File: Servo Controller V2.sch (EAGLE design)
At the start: 36 parts, among them P1 Power, IO, P2 Servo, P3 Program, Q1 BSS138, Q2 IRLML9301TRPBF, U1 ATTINY402-SSNR, U2 TPS82140SILR, U3 MCP1754ST-3302E_CB, U4 MCP1754ST-3302E_CB

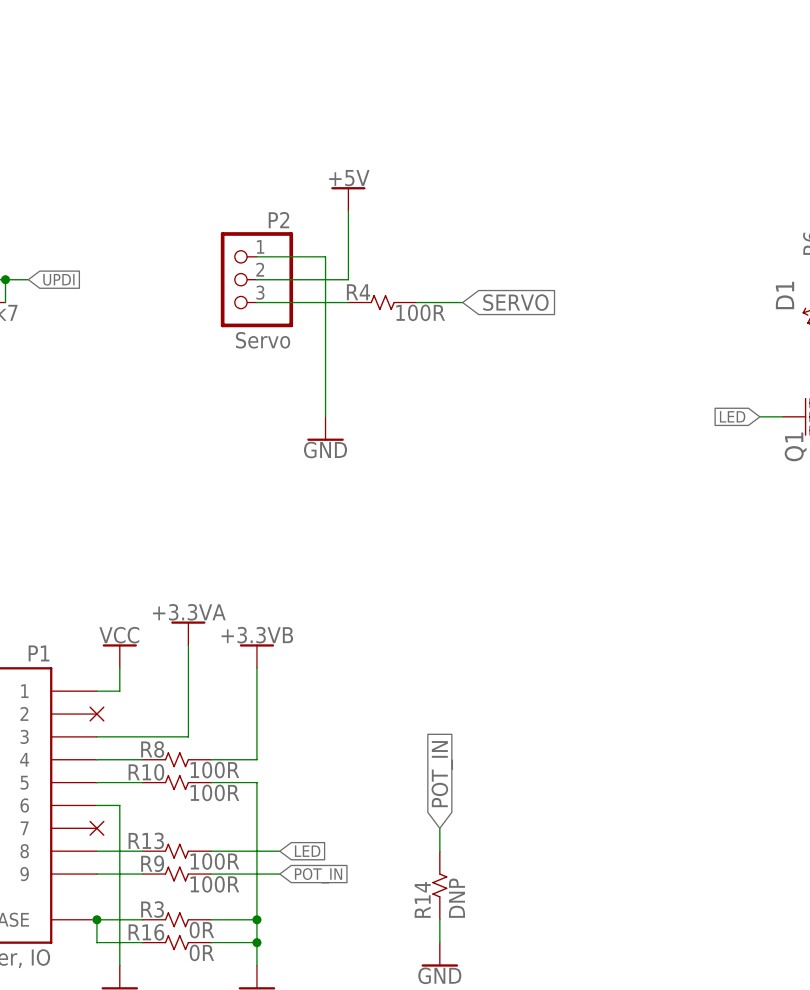
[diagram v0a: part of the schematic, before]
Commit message: Eliminated back EMI on the 5V rail from a large motor braking.
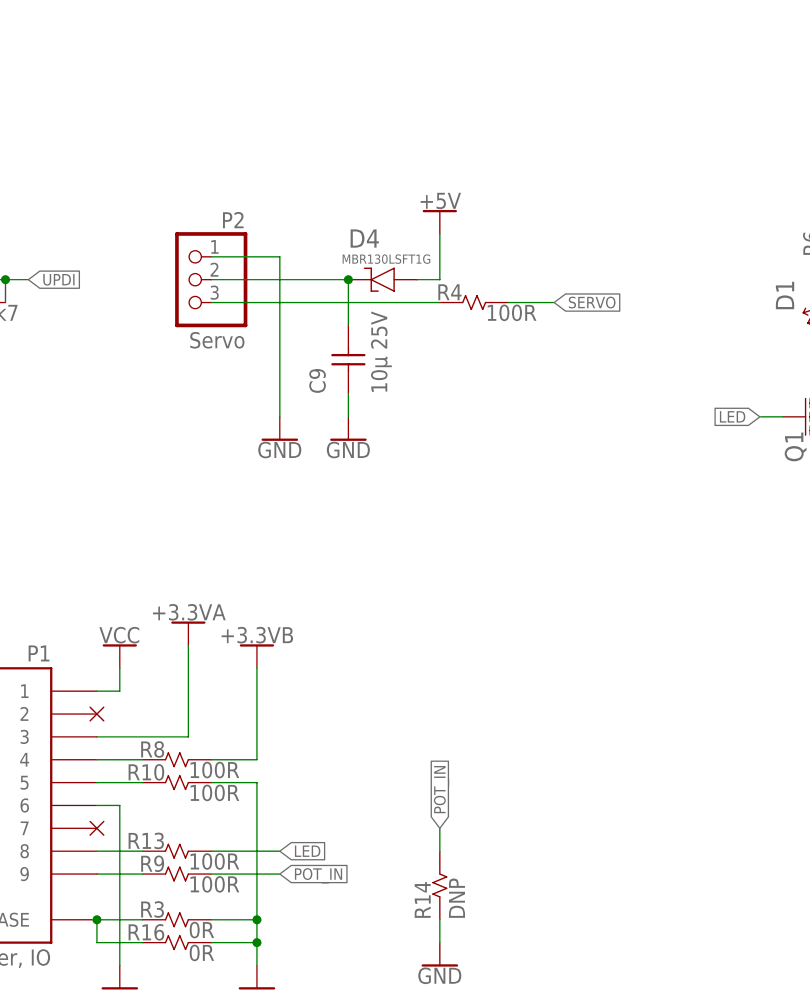
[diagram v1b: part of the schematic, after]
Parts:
- added C9: 10µ 25V, lcr:CAPACITOR-1206
- added D4: MBR130LSFT1G, lcr:DIODE-SCHOTTKY-ON-MBR130LSFT1G
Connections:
- new net N$19: C9.P$2, D4.C, P2.2
- net +5V: now also D4.A; no longer P2.2
- net GND: now also C9.P$1
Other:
- moved on the sheet: P2, R4
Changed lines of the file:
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@@
 <drawing>
 <settings>
-<setting alwaysvectorfont="no"/>
+<setting alwaysvectorfont="yes"/>
 <setting verticaltext="up"/>
 </settings>
@@
 <part name="P19" library="supply" library_urn="urn:adsk.eagle:library:8729613" deviceset="+5V" device=""/>
 <part name="P20" library="supply" library_urn="urn:adsk.eagle:library:8729613" deviceset="+5V" device=""/>
+<part name="C9" library="lcr" library_urn="urn:adsk.eagle:library:3920968" deviceset="CAPACITOR" device="-1206" package3d_urn="urn:adsk.eagle:package:4274891/1" value="10µ 25V"/>
+<part name="D4" library="lcr" library_urn="urn:adsk.eagle:library:3920968" deviceset="DIODE-SCHOTTKY" device="-ON-MBR130LSFT1G" package3d_urn="urn:adsk.eagle:package:4270842/1" value="MBR130LSFT1G"/>
+<part name="GND20" library="supply1" library_urn="urn:adsk.eagle:library:371" deviceset="GND" device=""/>
 </parts>
 <sheets>
@@
 <attribute name="VALUE" x="68.58" y="168.402" size="1.778" layer="96"/>
 </instance>
-<instance part="P2" gate="A" x="63.5" y="93.98" smashed="yes" rot="MR0">
-<attribute name="NAME" x="69.85" y="99.695" size="1.778" layer="95" rot="MR0"/>
-<attribute name="VALUE" x="69.85" y="86.36" size="1.778" layer="96" rot="MR0"/>
+<instance part="P2" gate="A" x="58.42" y="93.98" smashed="yes" rot="MR0">
+<attribute name="NAME" x="64.77" y="99.695" size="1.778" layer="95" rot="MR0"/>
+<attribute name="VALUE" x="64.77" y="86.36" size="1.778" layer="96" rot="MR0"/>
 </instance>
 <instance part="R1" gate="G$1" x="190.5" y="60.96" smashed="yes">
@@
 <attribute name="VALUE" x="248.92" y="55.626" size="1.778" layer="96" align="top-center"/>
 </instance>
-<instance part="GND12" gate="1" x="73.66" y="76.2" smashed="yes">
-<attribute name="VALUE" x="73.66" y="75.946" size="1.778" layer="96" align="top-center"/>
+<instance part="GND12" gate="1" x="68.58" y="76.2" smashed="yes">
+<attribute name="VALUE" x="68.58" y="75.946" size="1.778" layer="96" align="top-center"/>
 </instance>
 <instance part="GND13" gate="1" x="27.94" y="76.2" smashed="yes">
@@
 <attribute name="VALUE" x="58.42" y="36.068" size="1.778" layer="96"/>
 </instance>
-<instance part="R4" gate="G$1" x="81.28" y="91.44" smashed="yes">
-<attribute name="NAME" x="78.74" y="91.694" size="1.778" layer="95" rot="MR0"/>
-<attribute name="VALUE" x="81.28" y="89.408" size="1.778" layer="96"/>
+<instance part="R4" gate="G$1" x="91.44" y="91.44" smashed="yes">
+<attribute name="NAME" x="88.9" y="91.694" size="1.778" layer="95" rot="MR0"/>
+<attribute name="VALUE" x="91.44" y="89.408" size="1.778" layer="96"/>
 </instance>
 <instance part="R3" gate="G$1" x="58.42" y="22.86" smashed="yes">
@@
 <instance part="P17" gate="G$1" x="157.48" y="170.18" smashed="yes"/>
 <instance part="P18" gate="G$1" x="58.42" y="170.18" smashed="yes"/>
-<instance part="P19" gate="G$1" x="76.2" y="104.14" smashed="yes"/>
+<instance part="P19" gate="G$1" x="86.36" y="101.6" smashed="yes"/>
 <instance part="P20" gate="G$1" x="137.16" y="111.76" smashed="yes"/>
+<instance part="C9" gate="G$1" x="76.2" y="83.82" smashed="yes" rot="R90">
+<attribute name="NAME" x="73.66" y="81.28" size="1.778" layer="95" rot="R90"/>
+<attribute name="VALUE" x="80.518" y="81.28" size="1.778" layer="96" rot="R90"/>
+</instance>
+<instance part="D4" gate="G$1" x="81.28" y="93.98" smashed="yes" rot="MR0">
+<attribute name="NAME" x="76.2" y="97.536" size="2.032" layer="95"/>
+<attribute name="VALUE" x="75.438" y="95.758" size="1.016" layer="96"/>
+</instance>
+<instance part="GND20" gate="1" x="76.2" y="76.2" smashed="yes">
+<attribute name="VALUE" x="76.2" y="75.946" size="1.778" layer="96" align="top-center"/>
+</instance>
 </instances>
 <busses>
@@
 <pinref part="P2" gate="A" pin="1"/>
 <pinref part="GND12" gate="1" pin="GND"/>
-<wire x1="66.04" y1="96.52" x2="73.66" y2="96.52" width="0.1524" layer="91"/>
-<wire x1="73.66" y1="96.52" x2="73.66" y2="78.74" width="0.1524" layer="91"/>
+<wire x1="60.96" y1="96.52" x2="68.58" y2="96.52" width="0.1524" layer="91"/>
+<wire x1="68.58" y1="96.52" x2="68.58" y2="78.74" width="0.1524" layer="91"/>
 </segment>
 <segment>
@@
 <wire x1="22.86" y1="144.78" x2="22.86" y2="147.32" width="0.1524" layer="91"/>
 </segment>
+<segment>
+<pinref part="C9" gate="G$1" pin="P$1"/>
+<wire x1="76.2" y1="81.28" x2="76.2" y2="78.74" width="0.1524" layer="91"/>
+<pinref part="GND20" gate="1" pin="GND"/>
+</segment>
 </net>
 <net name="UPDI" class="0">
@@
 <wire x1="38.1" y1="93.98" x2="40.64" y2="93.98" width="0.1524" layer="91"/>
 <junction x="38.1" y="93.98"/>
-<label x="40.64" y="93.98" size="1.27" layer="255" xref="yes"/>
+<label x="40.64" y="93.98" size="1.27" layer="95" xref="yes"/>
 </segment>
 </net>
@@
 <pinref part="U1" gate="G$1" pin="PA7"/>
 <wire x1="193.04" y1="88.9" x2="187.96" y2="88.9" width="0.1524" layer="91"/>
-<label x="187.96" y="88.9" size="1.27" layer="255" rot="R180" xref="yes"/>
+<label x="187.96" y="88.9" size="1.27" layer="95" rot="R180" xref="yes"/>
 </segment>
 <segment>
@@
 <wire x1="218.44" y1="63.5" x2="218.44" y2="66.04" width="0.1524" layer="91"/>
 <wire x1="218.44" y1="66.04" x2="226.06" y2="66.04" width="0.1524" layer="91"/>
-<label x="226.06" y="66.04" size="1.27" layer="255" xref="yes"/>
+<label x="226.06" y="66.04" size="1.27" layer="95" xref="yes"/>
 </segment>
 </net>
@@
 <pinref part="U1" gate="G$1" pin="PA6"/>
 <wire x1="193.04" y1="91.44" x2="187.96" y2="91.44" width="0.1524" layer="91"/>
-<label x="187.96" y="91.44" size="1.27" layer="255" rot="R180" xref="yes"/>
+<label x="187.96" y="91.44" size="1.27" layer="95" rot="R180" xref="yes"/>
 </segment>
 <segment>
@@
 <wire x1="190.5" y1="63.5" x2="190.5" y2="66.04" width="0.1524" layer="91"/>
 <wire x1="190.5" y1="66.04" x2="198.12" y2="66.04" width="0.1524" layer="91"/>
-<label x="198.12" y="66.04" size="1.27" layer="255" xref="yes"/>
+<label x="198.12" y="66.04" size="1.27" layer="95" xref="yes"/>
 </segment>
 </net>
 <net name="POT_IN" class="0">
 <segment>
-<label x="187.96" y="86.36" size="1.27" layer="255" rot="R180" xref="yes"/>
+<label x="187.96" y="86.36" size="1.27" layer="95" rot="R180" xref="yes"/>
 <pinref part="U1" gate="G$1" pin="PA1"/>
 <wire x1="187.96" y1="86.36" x2="193.04" y2="86.36" width="0.1524" layer="91"/>
@@
 <pinref part="R9" gate="G$1" pin="P$2"/>
 <wire x1="60.96" y1="27.94" x2="68.58" y2="27.94" width="0.1524" layer="91"/>
-<label x="68.58" y="27.94" size="1.27" layer="255" xref="yes"/>
+<label x="68.58" y="27.94" size="1.27" layer="95" xref="yes"/>
 </segment>
 <segment>
 <pinref part="R14" gate="G$1" pin="P$2"/>
 <wire x1="86.36" y1="30.48" x2="86.36" y2="33.02" width="0.1524" layer="91"/>
-<label x="86.36" y="33.02" size="1.778" layer="95" rot="R90" xref="yes"/>
+<label x="86.36" y="33.02" size="1.27" layer="95" rot="R90" xref="yes"/>
 </segment>
 </net>
 <net name="SERVO" class="0">
 <segment>
-<label x="238.76" y="86.36" size="1.27" layer="255" xref="yes"/>
+<label x="238.76" y="86.36" size="1.27" layer="95" xref="yes"/>
 <pinref part="U1" gate="G$1" pin="PA2"/>
 <wire x1="238.76" y1="86.36" x2="233.68" y2="86.36" width="0.1524" layer="91"/>
@@
 <segment>
 <pinref part="R4" gate="G$1" pin="P$2"/>
-<wire x1="83.82" y1="91.44" x2="88.9" y2="91.44" width="0.1524" layer="91"/>
-<label x="88.9" y="91.44" size="1.778" layer="95" xref="yes"/>
+<wire x1="93.98" y1="91.44" x2="99.06" y2="91.44" width="0.1524" layer="91"/>
+<label x="99.06" y="91.44" size="1.27" layer="95" xref="yes"/>
 </segment>
 </net>
@@
 <pinref part="U1" gate="G$1" pin="PA3/EXTCLK"/>
 <wire x1="233.68" y1="91.44" x2="238.76" y2="91.44" width="0.1524" layer="91"/>
-<label x="238.76" y="91.44" size="1.27" layer="255" xref="yes"/>
+<label x="238.76" y="91.44" size="1.27" layer="95" xref="yes"/>
 </segment>
 <segment>
 <pinref part="Q1" gate="G$1" pin="G"/>
 <wire x1="124.46" y1="78.74" x2="121.92" y2="78.74" width="0.1524" layer="91"/>
-<label x="121.92" y="78.74" size="1.27" layer="255" rot="R180" xref="yes"/>
+<label x="121.92" y="78.74" size="1.27" layer="95" rot="R180" xref="yes"/>
 </segment>
 <segment>
 <pinref part="R13" gate="G$1" pin="P$2"/>
 <wire x1="60.96" y1="30.48" x2="68.58" y2="30.48" width="0.1524" layer="91"/>
-<label x="68.58" y="30.48" size="1.27" layer="255" xref="yes"/>
+<label x="68.58" y="30.48" size="1.27" layer="95" xref="yes"/>
 </segment>
 </net>
@@
 <pinref part="P2" gate="A" pin="3"/>
 <pinref part="R4" gate="G$1" pin="P$1"/>
-<wire x1="66.04" y1="91.44" x2="76.2" y2="91.44" width="0.1524" layer="91"/>
+<wire x1="60.96" y1="91.44" x2="86.36" y2="91.44" width="0.1524" layer="91"/>
 </segment>
 </net>
@@
 </segment>
 <segment>
-<pinref part="P2" gate="A" pin="2"/>
-<wire x1="66.04" y1="93.98" x2="76.2" y2="93.98" width="0.1524" layer="91"/>
-<wire x1="76.2" y1="93.98" x2="76.2" y2="101.6" width="0.1524" layer="91"/>
-<pinref part="P19" gate="G$1" pin="+5V"/>
-</segment>
-<segment>
 <pinref part="R6" gate="G$1" pin="P$2"/>
 <wire x1="129.54" y1="104.14" x2="129.54" y2="106.68" width="0.1524" layer="91"/>
@@
 <junction x="137.16" y="106.68"/>
 <pinref part="P20" gate="G$1" pin="+5V"/>
+</segment>
+<segment>
+<pinref part="D4" gate="G$1" pin="A"/>
+<wire x1="83.82" y1="93.98" x2="86.36" y2="93.98" width="0.1524" layer="91"/>
+<wire x1="86.36" y1="93.98" x2="86.36" y2="99.06" width="0.1524" layer="91"/>
+<pinref part="P19" gate="G$1" pin="+5V"/>
 </segment>
 </net>
@@
 </segment>
 </net>
+<net name="N$19" class="0">
+<segment>
+<pinref part="P2" gate="A" pin="2"/>
+<wire x1="60.96" y1="93.98" x2="76.2" y2="93.98" width="0.1524" layer="91"/>
+<pinref part="D4" gate="G$1" pin="C"/>
+<pinref part="C9" gate="G$1" pin="P$2"/>
+<wire x1="76.2" y1="93.98" x2="76.2" y2="88.9" width="0.1524" layer="91"/>
+<junction x="76.2" y="93.98"/>
+</segment>
+</net>

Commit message: Display OSHW logo on schematic.
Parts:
- added LOGO1: OSHW-LOGOMINI, SparkFun-Aesthetics:OSHW-LOGOMINI
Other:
- note added: "Schematic, PCB layout, and BOM released under GPLv3"
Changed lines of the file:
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@@
 <layer number="48" name="Document" color="7" fill="1" visible="no" active="no"/>
 <layer number="49" name="Reference" color="7" fill="1" visible="no" active="no"/>
+<layer number="50" name="dxf" color="7" fill="1" visible="no" active="no"/>
 <layer number="51" name="tDocu" color="7" fill="1" visible="no" active="no"/>
 <layer number="52" name="bDocu" color="7" fill="1" visible="no" active="no"/>
+<layer number="53" name="tGND_GNDA" color="7" fill="9" visible="no" active="no"/>
+<layer number="54" name="bGND_GNDA" color="1" fill="9" visible="no" active="no"/>
+<layer number="56" name="wert" color="7" fill="1" visible="no" active="no"/>
+<layer number="57" name="tCAD" color="7" fill="1" visible="no" active="no"/>
+<layer number="59" name="tCarbon" color="7" fill="1" visible="no" active="no"/>
+<layer number="60" name="bCarbon" color="7" fill="1" visible="no" active="no"/>
 <layer number="88" name="SimResults" color="9" fill="1" visible="yes" active="yes"/>
 <layer number="89" name="SimProbes" color="9" fill="1" visible="yes" active="yes"/>
@@
 <layer number="97" name="Info" color="7" fill="1" visible="yes" active="yes"/>
 <layer number="98" name="Guide" color="6" fill="1" visible="yes" active="yes"/>
+<layer number="99" name="SpiceOrder" color="7" fill="1" visible="no" active="no"/>
+<layer number="100" name="Muster" color="7" fill="1" visible="no" active="no"/>
+<layer number="101" name="Patch_Top" color="12" fill="4" visible="yes" active="yes"/>
+<layer number="102" name="Vscore" color="7" fill="1" visible="yes" active="yes"/>
+<layer number="103" name="tMap" color="7" fill="1" visible="yes" active="yes"/>
+<layer number="104" name="Name" color="16" fill="1" visible="yes" active="yes"/>
+<layer number="105" name="tPlate" color="7" fill="1" visible="yes" active="yes"/>
+<layer number="106" name="bPlate" color="7" fill="1" visible="yes" active="yes"/>
+<layer number="107" name="Crop" color="7" fill="1" visible="yes" active="yes"/>
+<layer number="108" name="tplace-old" color="10" fill="1" visible="yes" active="yes"/>
+<layer number="109" name="ref-old" color="11" fill="1" visible="yes" active="yes"/>
+<layer number="110" name="fp0" color="7" fill="1" visible="yes" active="yes"/>
+<layer number="111" name="LPC17xx" color="7" fill="1" visible="yes" active="yes"/>
+<layer number="112" name="tSilk" color="7" fill="1" visible="yes" active="yes"/>
+<layer number="113" name="IDFDebug" color="4" fill="1" visible="yes" active="yes"/>
+<layer number="114" name="Badge_Outline" color="7" fill="1" visible="no" active="yes"/>
+<layer number="115" name="ReferenceISLANDS" color="7" fill="1" visible="no" active="yes"/>
+<layer number="116" name="Patch_BOT" color="9" fill="4" visible="yes" active="yes"/>
+<layer number="118" name="Rect_Pads" color="7" fill="1" visible="no" active="yes"/>
+<layer number="121" name="_tsilk" color="7" fill="1" visible="yes" active="yes"/>
+<layer number="122" name="_bsilk" color="7" fill="1" visible="yes" active="yes"/>
+<layer number="123" name="tTestmark" color="7" fill="1" visible="yes" active="yes"/>
+<layer number="124" name="bTestmark" color="7" fill="1" visible="yes" active="yes"/>
+<layer number="125" name="_tNames" color="7" fill="1" visible="yes" active="yes"/>
+<layer number="126" name="_bNames" color="7" fill="1" visible="yes" active="yes"/>
+<layer number="127" name="_tValues" color="7" fill="1" visible="yes" active="yes"/>
+<layer number="128" name="_bValues" color="7" fill="1" visible="yes" active="yes"/>
+<layer number="129" name="Mask" color="7" fill="1" visible="yes" active="yes"/>
+<layer number="131" name="tAdjust" color="7" fill="1" visible="yes" active="yes"/>
+<layer number="132" name="bAdjust" color="7" fill="1" visible="yes" active="yes"/>
+<layer number="144" name="Drill_legend" color="7" fill="1" visible="yes" active="yes"/>
+<layer number="150" name="Notes" color="7" fill="1" visible="yes" active="yes"/>
+<layer number="151" name="HeatSink" color="7" fill="1" visible="yes" active="yes"/>
+<layer number="152" name="_bDocu" color="7" fill="1" visible="yes" active="yes"/>
+<layer number="153" name="FabDoc1" color="7" fill="1" visible="yes" active="yes"/>
+<layer number="154" name="FabDoc2" color="7" fill="1" visible="yes" active="yes"/>
+<layer number="155" name="FabDoc3" color="7" fill="1" visible="yes" active="yes"/>
+<layer number="199" name="Contour" color="7" fill="1" visible="yes" active="yes"/>
+<layer number="200" name="200bmp" color="1" fill="10" visible="yes" active="yes"/>
+<layer number="201" name="201bmp" color="2" fill="10" visible="yes" active="yes"/>
+<layer number="202" name="202bmp" color="3" fill="10" visible="yes" active="yes"/>
+<layer number="203" name="203bmp" color="4" fill="10" visible="yes" active="yes"/>
+<layer number="204" name="204bmp" color="5" fill="10" visible="yes" active="yes"/>
+<layer number="205" name="205bmp" color="6" fill="10" visible="yes" active="yes"/>
+<layer number="206" name="206bmp" color="7" fill="10" visible="yes" active="yes"/>
+<layer number="207" name="207bmp" color="8" fill="10" visible="yes" active="yes"/>
+<layer number="208" name="208bmp" color="9" fill="10" visible="yes" active="yes"/>
+<layer number="209" name="209bmp" color="7" fill="1" visible="yes" active="yes"/>
+<layer number="210" name="210bmp" color="7" fill="1" visible="yes" active="yes"/>
+<layer number="211" name="211bmp" color="7" fill="1" visible="yes" active="yes"/>
+<layer number="212" name="212bmp" color="7" fill="1" visible="yes" active="yes"/>
+<layer number="213" name="213bmp" color="7" fill="1" visible="yes" active="yes"/>
+<layer number="214" name="214bmp" color="7" fill="1" visible="yes" active="yes"/>
+<layer number="215" name="215bmp" color="7" fill="1" visible="yes" active="yes"/>
+<layer number="216" name="216bmp" color="7" fill="1" visible="yes" active="yes"/>
+<layer number="217" name="217bmp" color="18" fill="1" visible="no" active="no"/>
+<layer number="218" name="218bmp" color="19" fill="1" visible="no" active="no"/>
+<layer number="219" name="219bmp" color="20" fill="1" visible="no" active="no"/>
+<layer number="220" name="220bmp" color="21" fill="1" visible="no" active="no"/>
+<layer number="221" name="221bmp" color="22" fill="1" visible="no" active="no"/>
+<layer number="222" name="222bmp" color="23" fill="1" visible="no" active="no"/>
+<layer number="223" name="223bmp" color="24" fill="1" visible="no" active="no"/>
+<layer number="224" name="224bmp" color="25" fill="1" visible="no" active="no"/>
+<layer number="225" name="225bmp" color="7" fill="1" visible="yes" active="yes"/>
+<layer number="226" name="226bmp" color="7" fill="1" visible="yes" active="yes"/>
+<layer number="227" name="227bmp" color="7" fill="1" visible="yes" active="yes"/>
+<layer number="228" name="228bmp" color="7" fill="1" visible="yes" active="yes"/>
+<layer number="229" name="229bmp" color="7" fill="1" visible="yes" active="yes"/>
+<layer number="230" name="230bmp" color="7" fill="1" visible="yes" active="yes"/>
+<layer number="231" name="231bmp" color="7" fill="1" visible="yes" active="yes"/>
+<layer number="248" name="Housing" color="7" fill="1" visible="yes" active="yes"/>
+<layer number="249" name="Edge" color="7" fill="1" visible="yes" active="yes"/>
+<layer number="250" name="Descript" color="3" fill="1" visible="no" active="no"/>
+<layer number="251" name="SMDround" color="12" fill="11" visible="no" active="no"/>
+<layer number="254" name="cooling" color="7" fill="1" visible="yes" active="yes"/>
+<layer number="255" name="routoute" color="7" fill="1" visible="yes" active="yes"/>
 </layers>
 <schematic xreflabel="%F%N/%S.%C%R" xrefpart="/%S.%C%R">
@@
 <part name="U1" library="microchip-processors" deviceset="ATTINY402" device="" package3d_urn="urn:adsk.eagle:package:6770889/1" technology="-SSNR"/>
 <part name="U$1" library="frames" deviceset="LETTER-HORIZONTAL" device="">
-<attribute name="COMPANY_NAME" value=""/>
-<attribute name="PROJ_TITLE" value=""/>
-<attribute name="REVISION" value=""/>
+<attribute name="COMPANY_NAME" value="Andrew Russell"/>
+<attribute name="PROJ_TITLE" value="Experimental Avionics"/>
+<attribute name="REVISION" value="Rev 2"/>
 <attribute name="SCH_NAME" value="Full Schematic"/>
 </part>
@@
 <part name="D4" library="lcr" library_urn="urn:adsk.eagle:library:3920968" deviceset="DIODE-SCHOTTKY" device="-ON-MBR130LSFT1G" package3d_urn="urn:adsk.eagle:package:4270842/1" value="MBR130LSFT1G"/>
 <part name="GND20" library="supply1" library_urn="urn:adsk.eagle:library:371" deviceset="GND" device=""/>
+<part name="LOGO1" library="SparkFun-Aesthetics" library_urn="urn:adsk.eagle:library:507" deviceset="OSHW-LOGO" device="MINI" package3d_urn="urn:adsk.eagle:package:37101/1"/>
 </parts>
 <sheets>
@@
 <wire x1="47.498" y1="33.782" x2="49.022" y2="32.258" width="0.1524" layer="94"/>
 <wire x1="49.022" y1="33.782" x2="47.498" y2="32.258" width="0.1524" layer="94"/>
+<text x="200.66" y="2.54" size="1.778" layer="97" rot="MR0">Schematic, PCB layout, and BOM released under GPLv3</text>
 </plain>
 <instances>
@@
 <attribute name="VALUE" x="76.2" y="75.946" size="1.778" layer="96" align="top-center"/>
 </instance>
+<instance part="LOGO1" gate="G$1" x="170.18" y="17.78" smashed="yes"/>
 </instances>
 <busses>
